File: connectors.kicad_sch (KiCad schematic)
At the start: 4 parts, among them J1 Conn_01x04_Pin, J2 Conn_01x04_Pin, J3 Conn_01x09_Pin, J4 Conn_02x03_Odd_Even

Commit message: Completed symbol footprints.
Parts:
- J1, J2: footprint (none) -> Connector_PinHeader_2.54mm:PinHeader_1x04_P2.54mm_Vertical
- J3: footprint (none) -> Connector_PinHeader_2.54mm:PinHeader_1x09_P2.54mm_Vertical
- J4: footprint (none) -> Connector_PinHeader_2.54mm:PinHeader_2x03_P2.54mm_Vertical
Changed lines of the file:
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@@
 			)
 		)
-		(property "Footprint" ""
+		(property "Footprint" "Connector_PinHeader_2.54mm:PinHeader_1x04_P2.54mm_Vertical"
 			(at 107.95 73.66 0)
 			(effects
@@
 			)
 		)
-		(property "Footprint" ""
+		(property "Footprint" "Connector_PinHeader_2.54mm:PinHeader_1x09_P2.54mm_Vertical"
 			(at 78.74 118.11 0)
 			(effects
@@
 			)
 		)
-		(property "Footprint" ""
+		(property "Footprint" "Connector_PinHeader_2.54mm:PinHeader_2x03_P2.54mm_Vertical"
 			(at 118.11 119.38 0)
 			(effects
@@
 			)
 		)
-		(property "Footprint" ""
+		(property "Footprint" "Connector_PinHeader_2.54mm:PinHeader_1x04_P2.54mm_Vertical"
 			(at 74.93 72.39 0)
 			(effects

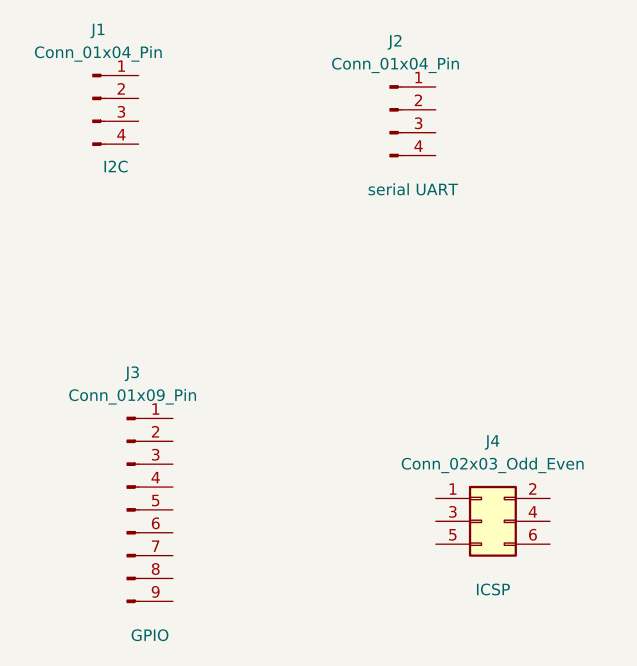
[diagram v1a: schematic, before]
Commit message: complete wiring in 2nd page.
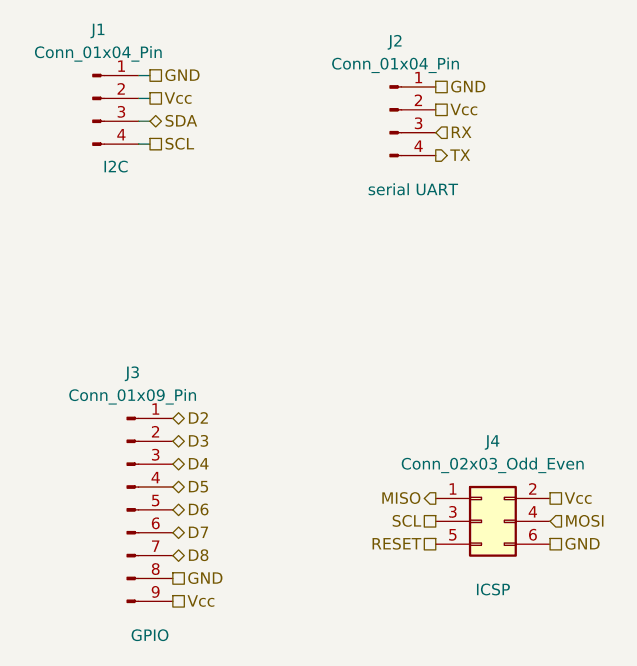
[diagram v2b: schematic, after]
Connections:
- net GND: now reaches J2.1 (Pin_1)
- net GND: now also J1.1 (Pin_1), J3.8 (Pin_8), J4.6 (Pin_6)
- net Vcc: now reaches J2.2 (Pin_2)
- net Vcc: now also J1.2 (Pin_2), J3.9 (Pin_9), J4.2 (Pin_2)
- net RX: now reaches J2.3 (Pin_3)
- net TX: now reaches J2.4 (Pin_4)
- net D2: now reaches J3.1 (Pin_1)
- net D3: now reaches J3.2 (Pin_2)
- net D4: now reaches J3.3 (Pin_3)
- net D5: now reaches J3.4 (Pin_4)
- net D6: now reaches J3.5 (Pin_5)
- net D7: now reaches J3.6 (Pin_6)
- net D8: now reaches J3.7 (Pin_7)
- net MISO: now reaches J4.1 (Pin_1)
- net SCL: now reaches J4.3 (Pin_3)
- net SCL: now also J1.4 (Pin_4)
- net MOSI: now reaches J4.4 (Pin_4)
- net RESET: now reaches J4.5 (Pin_5)
- net SDA: now reaches J1.3 (Pin_3)
